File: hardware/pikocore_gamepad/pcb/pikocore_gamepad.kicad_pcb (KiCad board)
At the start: 4 copper layers, 100 x 80 mm, 128 parts, among them J1 PHONES, J2 USB-C, J3 LiPo, J4 LCD_FPC, J5 SPEAKER 8R, Q1 2N7002, SW1 DPAD_UP, SW10 BTN_R, SW11 BTN_START, SW12 BTN_SELECT, SW13 BOOTSEL, SW14 RUN, SW15 PWR, SW2 DPAD_DOWN, SW3 DPAD_LEFT, SW4 DPAD_RIGHT, SW5 BTN_X, SW6 BTN_Y, SW7 BTN_A, SW8 BTN_B, SW9 BTN_L, U1 RP2350A, U2 TPS61023DRLR, U3 PT2308-S, U4 PAM8302A, U5 PCM5102APWR, U6 W25Q128JVSIQ, U7 TPS63001DRCR, U8 ETA6096D3K, Y1 12MHz

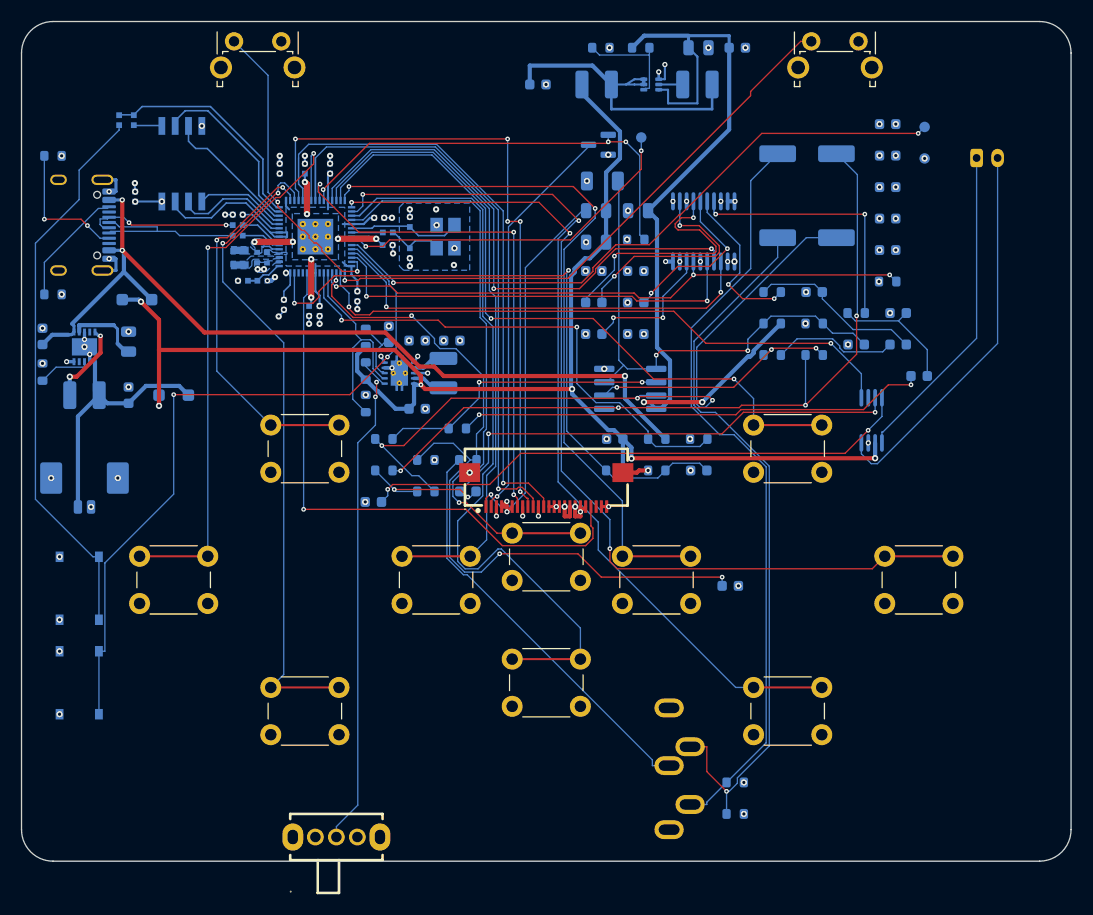
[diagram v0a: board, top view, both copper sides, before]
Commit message: hw: dorso de 100x60: jacks arriba, USB abajo, nucleo detras del panel, audio y TPS en la banda inferior
Co-Authored-By: Claude Fable 5.1 <noreply@anthropic.com>
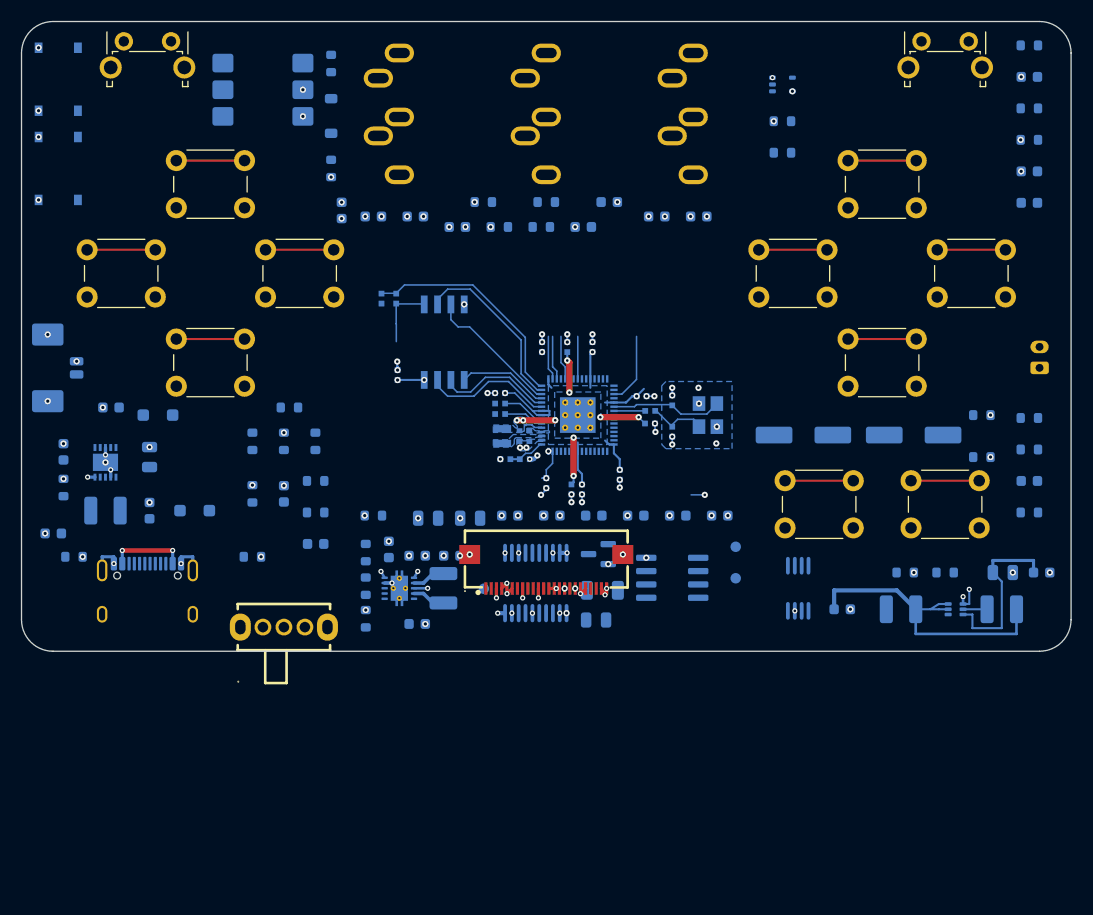
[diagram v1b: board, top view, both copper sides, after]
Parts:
- added C56: 100nF, Capacitor_SMD:C_0603_1608Metric, B.Cu at (30.5, 18.0)
- added D3: 1N4148W, Diode_SMD:D_SOD-123, B.Cu at (29.5, 9.00)
- added J6: MIDI IN, Connector_Audio:Jack_3.5mm_CUI_SJ1-3535NG_Horizontal, B.Cu at (36.0, 3.00)
- added J7: MIDI OUT, Connector_Audio:Jack_3.5mm_CUI_SJ1-3535NG_Horizontal, B.Cu at (64.0, 3.00)
- added R40: 33R, Resistor_SMD:R_0603_1608Metric, B.Cu at (72.5, 9.50)
- added R41: 10R, Resistor_SMD:R_0603_1608Metric, B.Cu at (72.5, 12.5)
- added R42: 220R, Resistor_SMD:R_0603_1608Metric, B.Cu at (29.5, 4.00)
- added R43: 4.7k, Resistor_SMD:R_0603_1608Metric, B.Cu at (29.5, 14.0)
- added U10: H11L1M, Package_DIP:SMDIP-6_W7.62mm, B.Cu at (23.0, 6.50)
- added U9: 74LVC1G17, Package_TO_SOT_SMD:SOT-353_SC-70-5, B.Cu at (72.5, 6.00)
- moved J1 74.9 mm to (50.0, 3.00), turned to 180 degrees
- moved TP3 58.7 mm to (44.0, 54.0)
- moved C4 57.8 mm to (78.2, 56.0)
- moved C5 57.8 mm to (93.5, 52.5)
- moved C7 57.8 mm to (97.2, 52.5)
- moved L1 57.8 mm to (93.4, 56.0)
- moved L2 57.8 mm to (83.8, 56.0)
- moved R4 57.8 mm to (88.0, 52.5)
- moved R5 57.8 mm to (84.2, 52.5)
- moved U2 57.8 mm to (89.0, 56.0)
- moved SW14 57.5 mm to (3.50, 5.50)
- moved R13 55.1 mm to (96.0, 46.8)
- moved C27 54.3 mm to (3.02, 48.8)
- moved C12 49.8 mm to (33.5, 18.6)
- moved TP2 46.6 mm to (68.0, 53.0)
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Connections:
- U1 pad 36: VBUS_SENSE -> MIDI_TX
- U1 pad 37: unconnected-(U1-GPIO25-Pad37) -> MIDI_RX
- U1 pad 41: unconnected-(U1-GPIO27-Pad41) -> VBUS_SENSE
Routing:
- net VSYS: track 137.1 -> 0.00 mm, vias 6 -> 0
- net BTN_A: track 89.5 -> 6.50 mm, vias 3 -> 0
- net BTN_B: track 84.7 -> 6.50 mm, vias 2 -> 0
- net VBUS: track 85.0 -> 7.31 mm, vias 3 -> 2
- net AUDIO_L: track 75.0 -> 0.00 mm, vias 4 -> 0
- net JACK_DET: track 74.7 -> 0.00 mm, vias 4 -> 0
- net JACK_L: track 73.1 -> 0.00 mm
- net JACK_R: track 70.4 -> 0.00 mm, vias 1 -> 0
- net RUN: track 68.3 -> 0.00 mm, vias 2 -> 0
- net AUDIO_R: track 68.2 -> 0.00 mm, vias 3 -> 0
- net 5V: track 79.7 -> 16.8 mm, vias 2 -> 0
- net LCD_SCK: track 62.8 -> 0.00 mm, vias 5 -> 0
- net SWDIO: track 62.6 -> 0.00 mm, vias 2 -> 0
- net BTN_Y: track 69.0 -> 6.50 mm, vias 2 -> 0
- net VSYS_ADC: track 62.1 -> 0.00 mm, vias 2 -> 0
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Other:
- board size 100 x 80 mm -> 100 x 60 mm

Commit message: hw: ruteo de la placa 100x60 con MIDI (DRC 0 errores, 0 sin conectar)
El nucleo RP2350A gira a rot 270 para que la fila de pines del LCD, I2S_DIN, D-pad y X/Y/A/B mire al flex y al DAC: a rot 90 freerouting se estancaba con 5-7 de esas senales sin rutear. DAC y op-amp salen del pasillo de los carriles del LCD; pads SWD anclados en la columna derecha.

Co-Authored-By: Claude Fable 5.1 <noreply@anthropic.com>
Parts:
- moved R14 70.6 mm to (96.0, 40.8)
- moved TP3 69.5 mm to (97.0, 9.00), turned to 0 degrees
- moved R16 68.0 mm to (96.0, 43.8)
- moved R17 68.0 mm to (96.0, 46.8)
- moved R9 55.7 mm to (41.5, 19.6)
- moved TP1 55.2 mm to (97.0, 3.00), turned to 0 degrees
- moved TP2 55.2 mm to (97.0, 6.00), turned to 0 degrees
- moved R10 51.2 mm to (45.5, 19.6)
- moved C20 46.8 mm to (49.5, 19.6)
- moved C21 42.6 mm to (53.5, 19.6)
- moved C13 39.1 mm to (66.5, 44.8)
- moved C12 39.1 mm to (62.5, 44.8)
- moved R8 39.1 mm to (60.5, 18.6)
- moved R6 35.2 mm to (66.5, 47.8)
- moved C16 35.2 mm to (62.5, 47.8)
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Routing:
- net VSYS: track 0.00 -> 102.6 mm, vias 0 -> 6
- net 5V: track 16.8 -> 116.0 mm, vias 0 -> 4
- net VREF25: track 0.00 -> 90.9 mm
- net AUDIO_L: track 0.00 -> 90.9 mm, vias 0 -> 3
- net OPL_N: track 0.00 -> 84.6 mm, vias 0 -> 2
- net SWCLK: track 0.00 -> 78.9 mm, vias 0 -> 2
- net USB_BOOT: track 0.00 -> 77.8 mm, vias 0 -> 2
- net SPK_SUM: track 0.00 -> 76.5 mm, vias 0 -> 2
- net SWDIO: track 0.00 -> 67.9 mm, vias 0 -> 2
- net SPK_SHDN: track 0.00 -> 66.2 mm, vias 0 -> 2
- net DACOUT_L: track 0.00 -> 65.9 mm, vias 0 -> 4
- net USB_DM: track 0.00 -> 65.5 mm, vias 0 -> 4
- net BB_PS: track 0.00 -> 64.1 mm, vias 0 -> 2
- net JACK_L: track 0.00 -> 63.3 mm, vias 0 -> 2
- net AUDIO_R: track 0.00 -> 63.3 mm
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
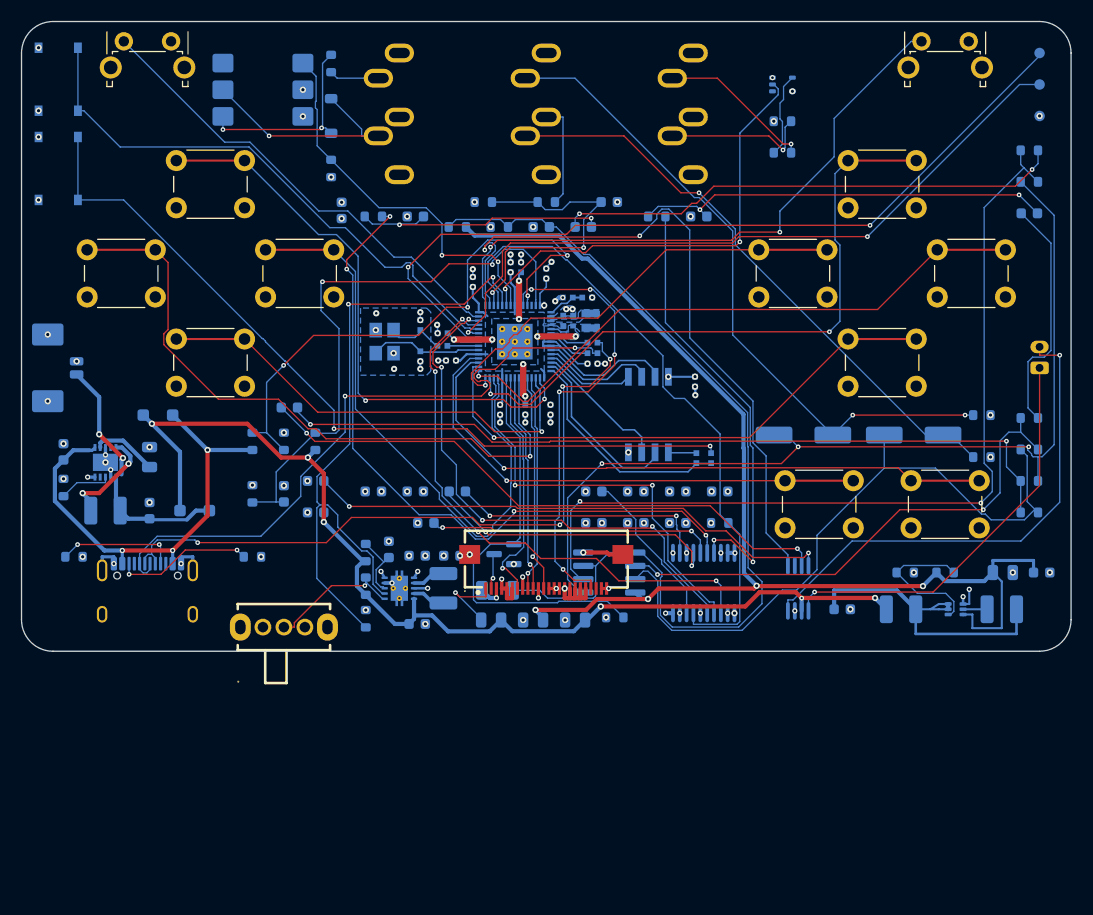
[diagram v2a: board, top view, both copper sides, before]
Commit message: hw: pase de correcciones de la revision final (MIDI IN, pines del firmware, nucleo)
- MIDI IN tenia Tip y Ring al reves respecto de la norma: el emisor pone
  corriente por DIN 4 (= Ring en tipo A); ahora Ring -> 220R -> anodo del
  H11L1 y Tip -> catodo. Solo hubiera recibido de equipos tipo B.
- El firmware PIKO_GAMEPAD usaba GP25 (ahora MIDI_RX) como LED y GP27
  (VBUS_SENSE) como clock-in: LED y trigger-out quedan en -1 con guardas en
  main.cpp, el clock-in pasa a GP28. Test nuevo que cruza los literales de
  hw_gamepi13.h contra pinmap.py. Compila.
- Una sola caja medida del nucleo (NUCLEO_BOX) para tests y comentarios.
- route_io.py apaga los asserts de wx: ExportSpecctraDSN abria un dialogo
  modal y colgaba el ciclo. Carriles copiados hasta 12.5mm; bajadas manuales
  de LCD_DC y LCD_MOSI a J4 y de PWR_EN al slide; BTN_START sin carril.

Puertas: 210 tests, ERC 0/0, DRC 0 errores / 0 sin conectar / 0 paridad
(15 avisos), G-0 en rojo solo por LCD_FPC_PIN_ORDER.

Co-Authored-By: Claude Fable 5.1 <noreply@anthropic.com>
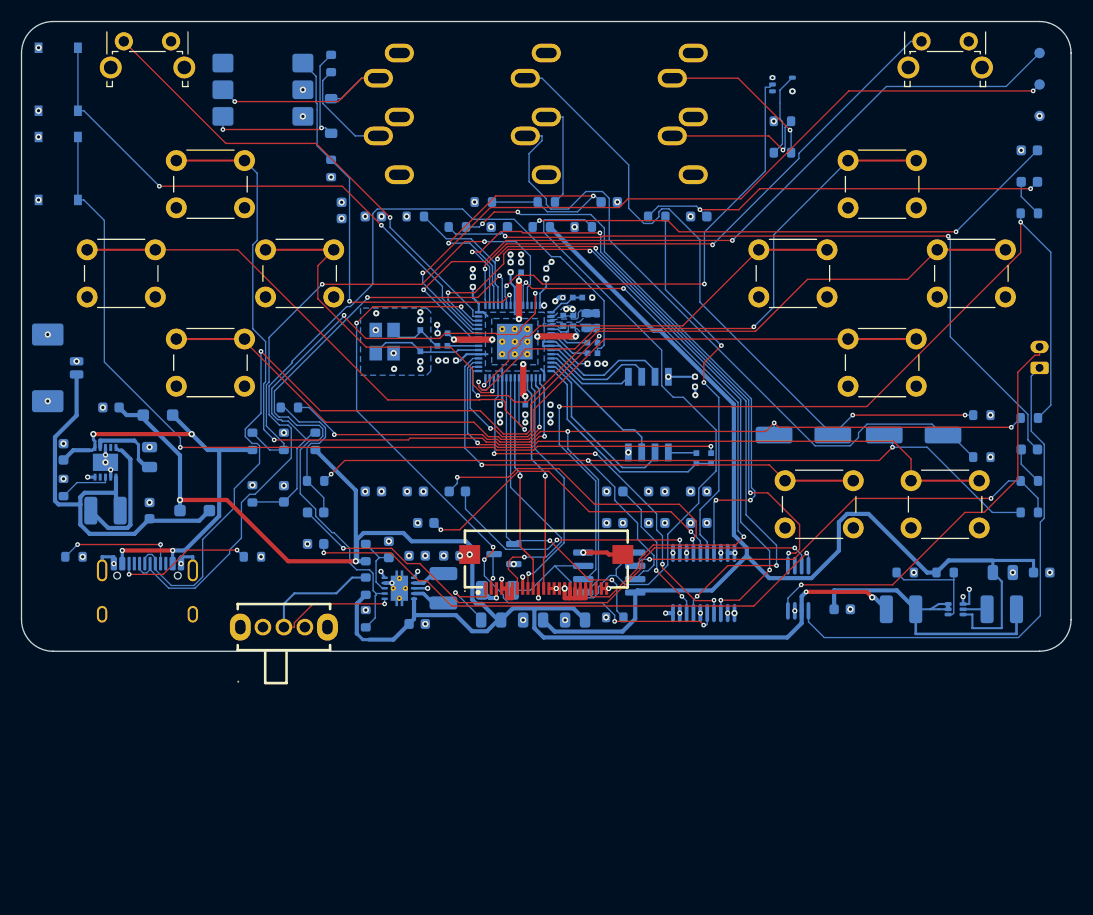
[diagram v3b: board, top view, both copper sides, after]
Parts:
- moved R16 70.8 mm to (25.5, 36.8)
- moved R17 68.1 mm to (28.0, 43.8)
- moved C20 47.1 mm to (96.0, 12.3)
- moved C21 42.7 mm to (96.0, 15.3)
- moved C16 41.2 mm to (33.5, 18.6)
- moved R6 41.2 mm to (37.5, 18.6)
- moved C17 27.0 mm to (64.5, 18.6)
- moved R7 27.0 mm to (60.5, 18.6)
- moved C22 22.5 mm to (96.0, 40.8)
- moved R12 22.5 mm to (96.0, 37.8)
- moved C27 21.9 mm to (8.53, 36.8)
- moved C18 19.0 mm to (45.5, 19.6)
- moved R8 19.0 mm to (41.5, 19.6)
- moved C13 10.4 mm to (56.5, 47.8)
- moved C25 10.3 mm to (28.0, 46.8)
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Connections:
- J6 pad R: MIDI_IN_K -> MIDI_IN_R
- J6 pad T: MIDI_IN_T -> MIDI_IN_K
- R42 pad 1: MIDI_IN_T -> MIDI_IN_R
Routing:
- net SPK_SUM: track 76.5 -> 15.0 mm, vias 2 -> 0
- net INL: track 48.4 -> 3.66 mm, vias 2 -> 0
- net VSYS: track 102.6 -> 138.5 mm, vias 6 -> 4
- net VREF25: track 90.9 -> 125.3 mm, vias 0 -> 2
- net AOUT_R: track 39.9 -> 72.8 mm
- net DACOUT_L: track 65.9 -> 36.6 mm, vias 4 -> 2
- net AUDIO_R: track 63.3 -> 86.6 mm, vias 0 -> 3
- net DPAD_RIGHT: track 57.5 -> 34.3 mm, vias 0 -> 1
- net USB_DP: track 62.3 -> 84.1 mm, vias 2 -> 0
- net INR: track 22.6 -> 3.66 mm
- net I2S_LRCK: track 51.0 -> 67.5 mm, vias 4 -> 6
- net LCD_TE: track 43.6 -> 58.4 mm, vias 5 -> 3
- net VBAT: track 24.7 -> 38.7 mm, vias 2 -> 0
- net AOUT_L: track 25.6 -> 39.7 mm
- net DACOUT_R: track 42.2 -> 54.8 mm, vias 2 -> 4
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
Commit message: hw: codigos LCSC de las piezas del MIDI, verificados en lcsc.com
C22859 10R, C23140 33R, C22962 220R (UNI-ROYAL 0603 1%), C81598 1N4148W
(ST Semtech, SOD-123), C10425 SN74LVC1G17DCKR (SC-70-5), C20082
H11L1SR2M (onsemi, gull-wing SMD en carrete; el C16587 es el DIP
pasante). El paquete de fab queda con las 20 lineas sin codigo que ya
tenia main (piezas de soldadura manual).

Co-Authored-By: Claude Fable 5.1 <noreply@anthropic.com>
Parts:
- U10: value H11L1M -> H11L1SR2M
- U9: value 74LVC1G17 -> SN74LVC1G17DCKR
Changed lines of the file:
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@@
 			)
 		)
-		(property "Value" "H11L1M"
+		(property "Value" "H11L1SR2M"
 			(at 0 -4.87 180)
 			(layer "Cmts.User")
@@
 			)
 		)
-		(property "Value" "74LVC1G17"
+		(property "Value" "SN74LVC1G17DCKR"
 			(at 0 -2 180)
 			(layer "Cmts.User")

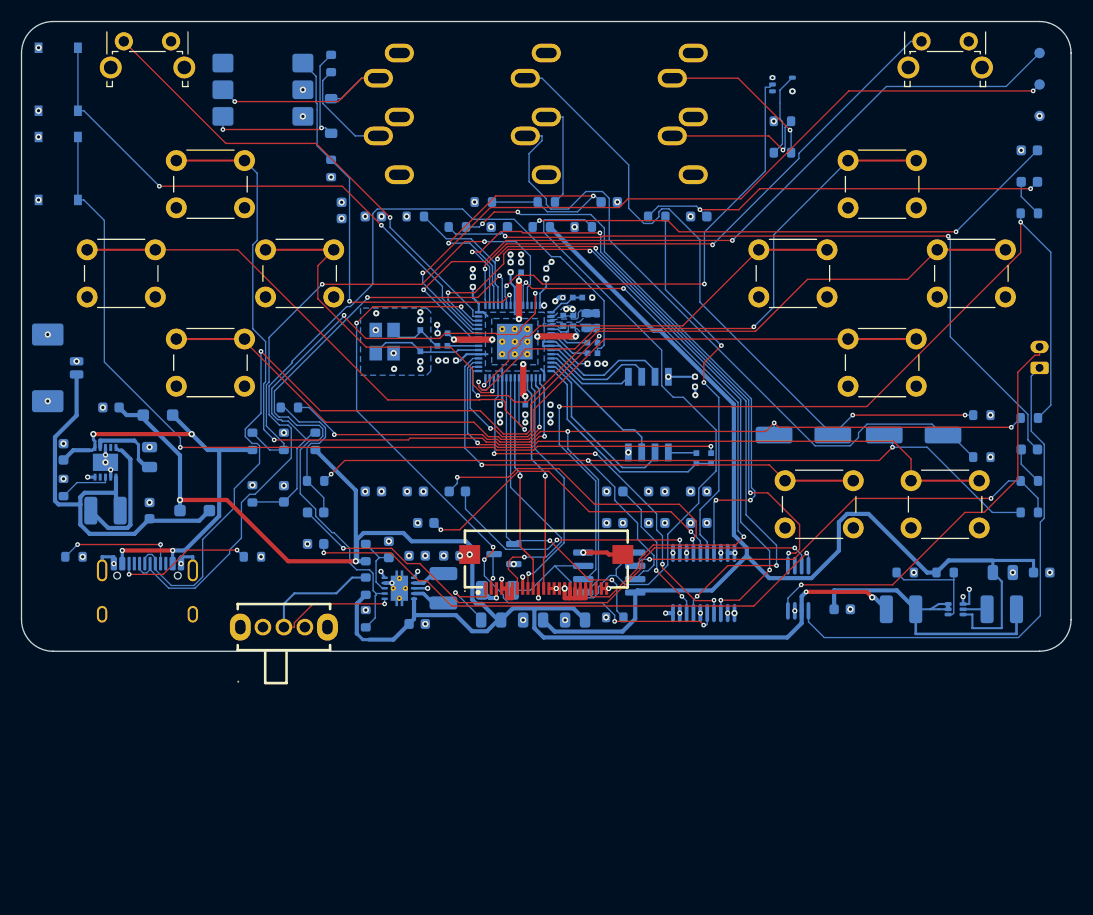
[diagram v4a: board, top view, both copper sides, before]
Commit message: hw: bateria con conector JST GH (las celdas del usuario no son MX1.25)
J3 pasa de Molex PicoBlade a JST GH BM02B-GHS-TBT (1.25mm, vertical SMD,
con traba), LCSC C161690 verificado en lcsc.com. Las celdas del usuario
traen GH, que no entra en el PicoBlade aunque tenga el mismo paso.
Posicion corrida a x 4.6 por el courtyard mas ancho; ciclo de ruteo
completo, DRC 0 errores / 0 sin conectar / 0 paridad.

Co-Authored-By: Claude Sonnet 5.5 <noreply@anthropic.com>
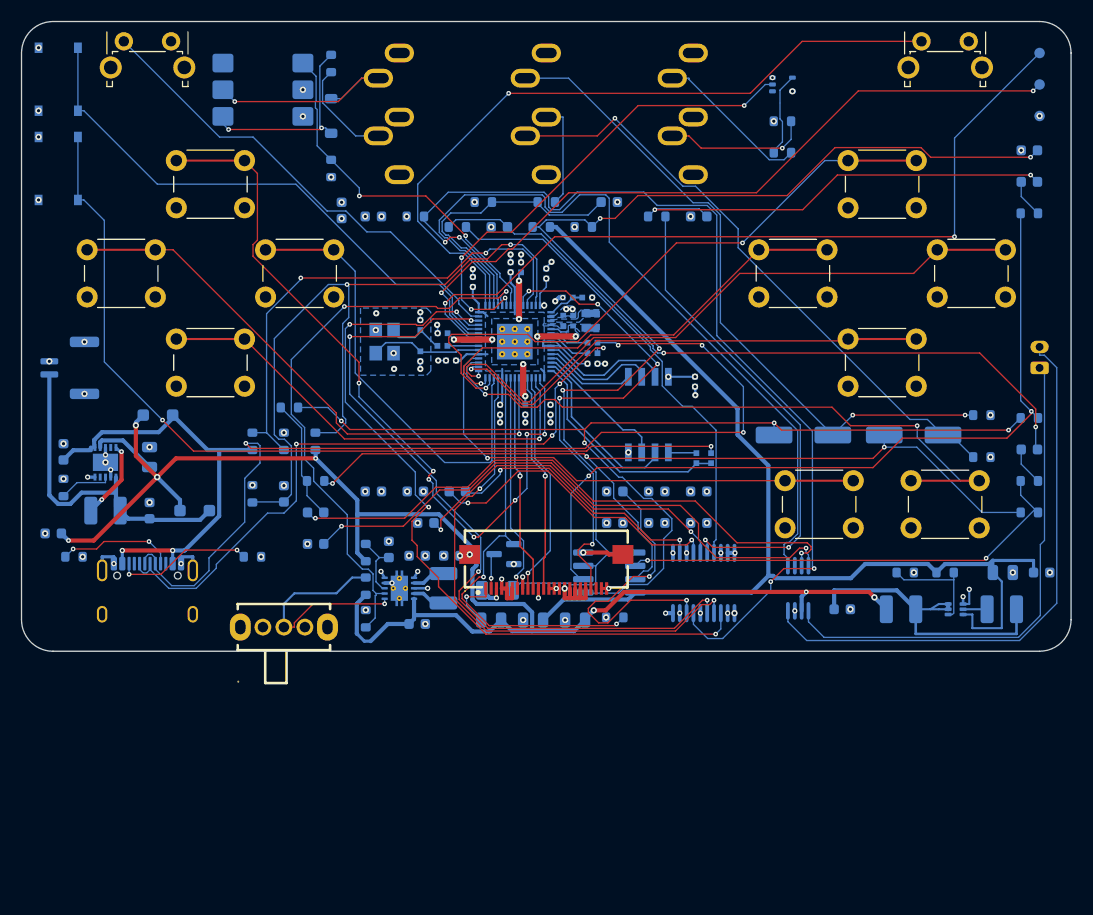
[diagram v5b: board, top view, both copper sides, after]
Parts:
- J3: footprint Connector_Molex:Molex_PicoBlade_53398-0271_1x02-1MP_P1.25mm_Vertical -> Connector_JST:JST_GH_BM02B-GHS-TBT_1x02-1MP_P1.25mm_Vertical
- moved C27 13.2 mm to (3.02, 48.8)
- moved J3 0.60 mm to (4.60, 33.0)
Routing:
- net DAC_XSMT: track 71.2 -> 98.5 mm
- net USB_DP: track 84.1 -> 62.7 mm, vias 0 -> 4
- net VSYS_ADC: track 51.1 -> 70.5 mm
- net USB_DM: track 75.1 -> 93.0 mm, vias 2 -> 4
- net OPL_N: track 92.7 -> 76.2 mm
- net LDOO: track 14.2 -> 28.9 mm
- net BTN_R: track 54.6 -> 68.7 mm, vias 2 -> 1
- net I2S_DIN: track 38.1 -> 51.4 mm, vias 4 -> 2
- net VREF25: track 125.3 -> 112.3 mm, vias 2 -> 4
- net SPK_N: track 41.5 -> 54.2 mm, vias 1 -> 0
- net SPK_SHDN: track 60.4 -> 73.1 mm, vias 4 -> 0
- net DACOUT_L: track 36.6 -> 46.9 mm
- net LCD_BLK: track 31.2 -> 41.2 mm
- net LCD_TE: track 58.4 -> 48.4 mm, vias 3 -> 5
- net DACOUT_R: track 54.8 -> 45.1 mm, vias 4 -> 0
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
